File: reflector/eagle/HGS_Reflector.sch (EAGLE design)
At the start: 20 parts, among them J1 U.FL, U1 TQP3M9037, U2 TQP3M903X, U3 LP2985XX-N

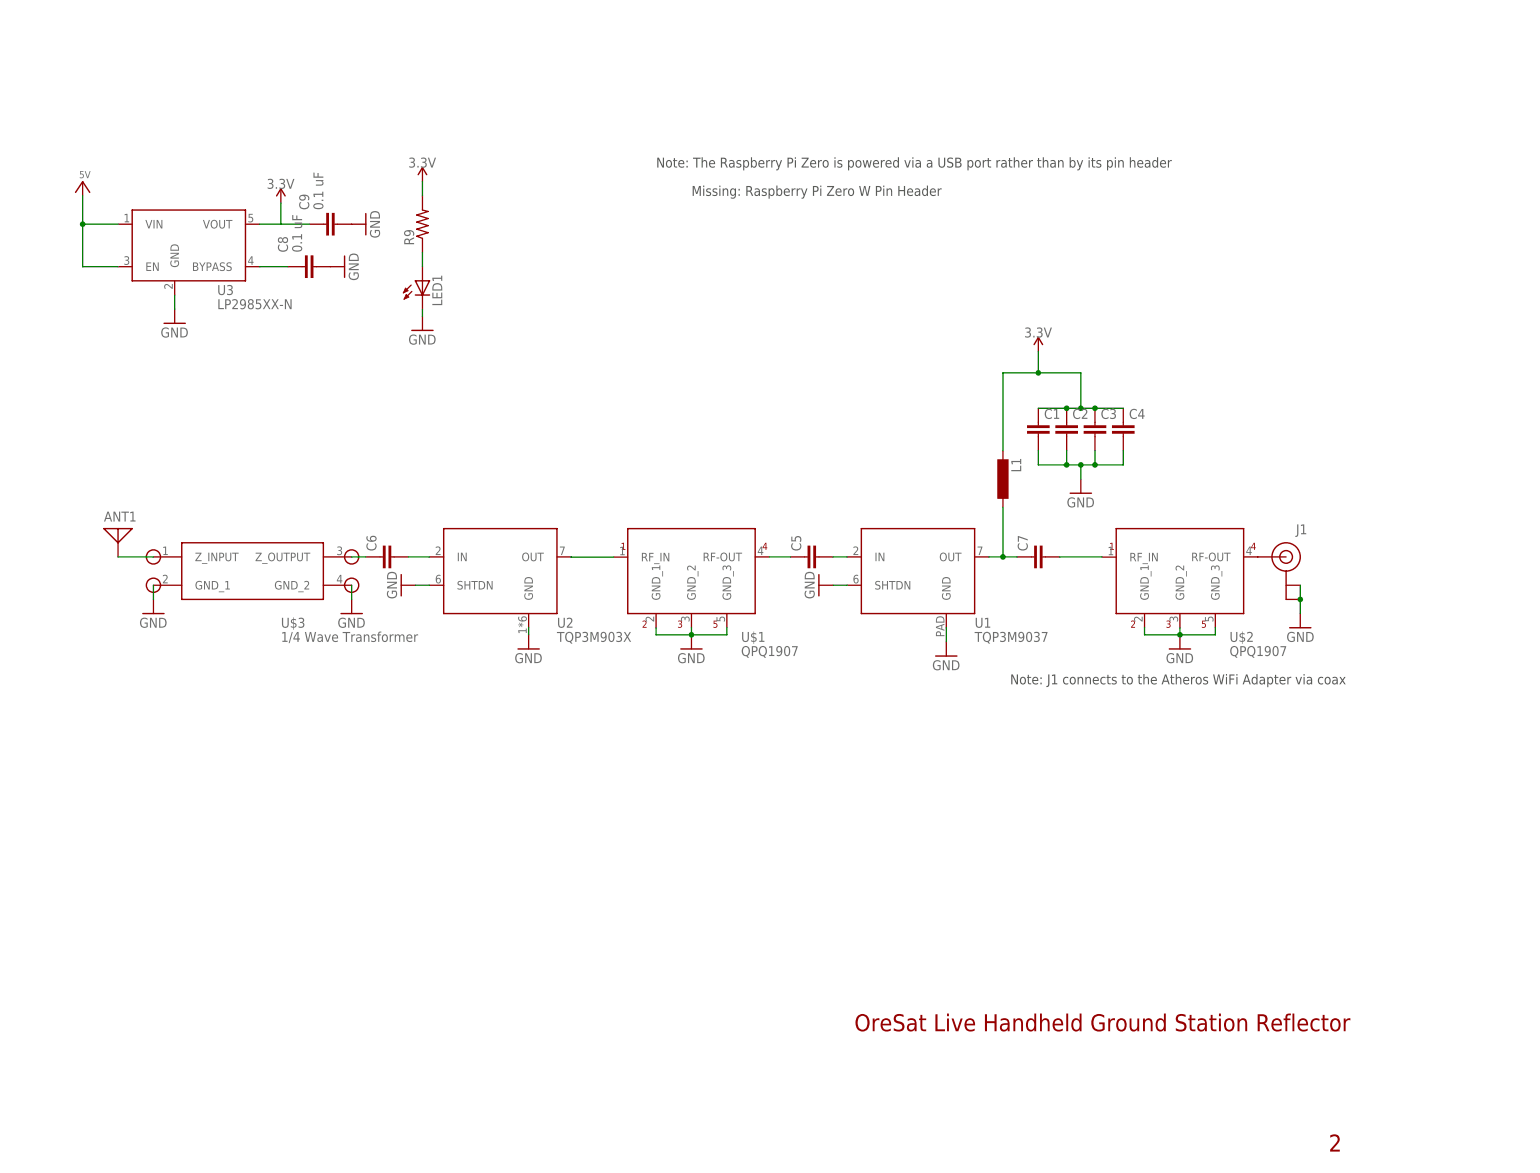
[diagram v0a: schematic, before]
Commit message: Fixed sch/brd inconsistancy
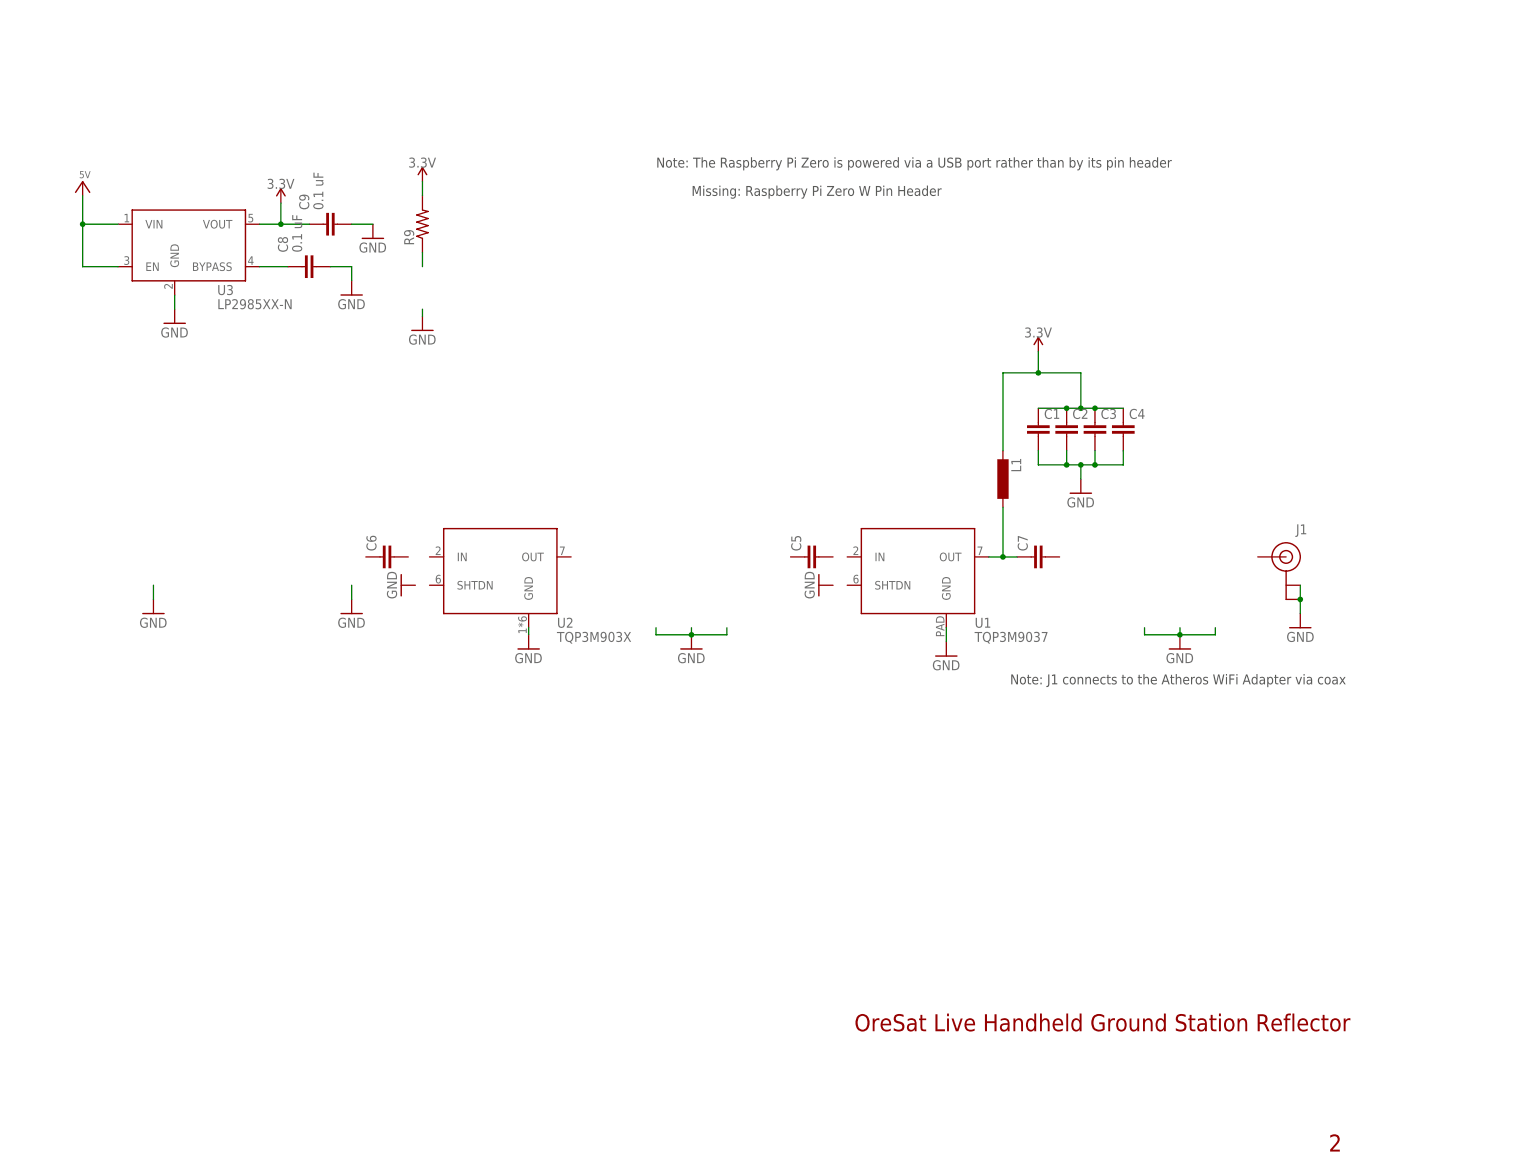
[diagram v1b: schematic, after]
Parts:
- removed ANT1: (no value), discrete:ANTENNA
- removed LED1: (no value), eagle-ltspice:LED_E
- removed U$1, U$2: BPFQPQ1907, HGS_Data_Parts:BPFQPQ1907
- removed U$3: 1/4_WAVE_TRF, HGS_Data_Parts:1/4_WAVE_TRF
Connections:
- removed net N$1 (its old number): C5.2, U1.IN
- removed net N$11: ANT1.1, U$3.Z_INPUT
- removed net N$2: U$1.RF_IN, U2.OUT
- removed net N$3: C5.1, U$1.RF-OUT
- removed net N$4: C7.2
- removed net N$6: J1.SIGNAL, U$2.RF-OUT
- removed net N$7: C6.1, U$3.Z_OUTPUT
- removed net N$8: C6.2, U2.IN
- removed net N$9: U$3.GND_2
- net GND: no longer LED1.C, U$1.GND_1, U$1.GND_2, U$1.GND_3, U$2.GND_1, U$2.GND_2, U$2.GND_3, U$3.GND_1, U1.SHTDN, U2.SHTDN
- net N$10: no longer LED1.A

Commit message: Completed schematic with respect to the current block diagram
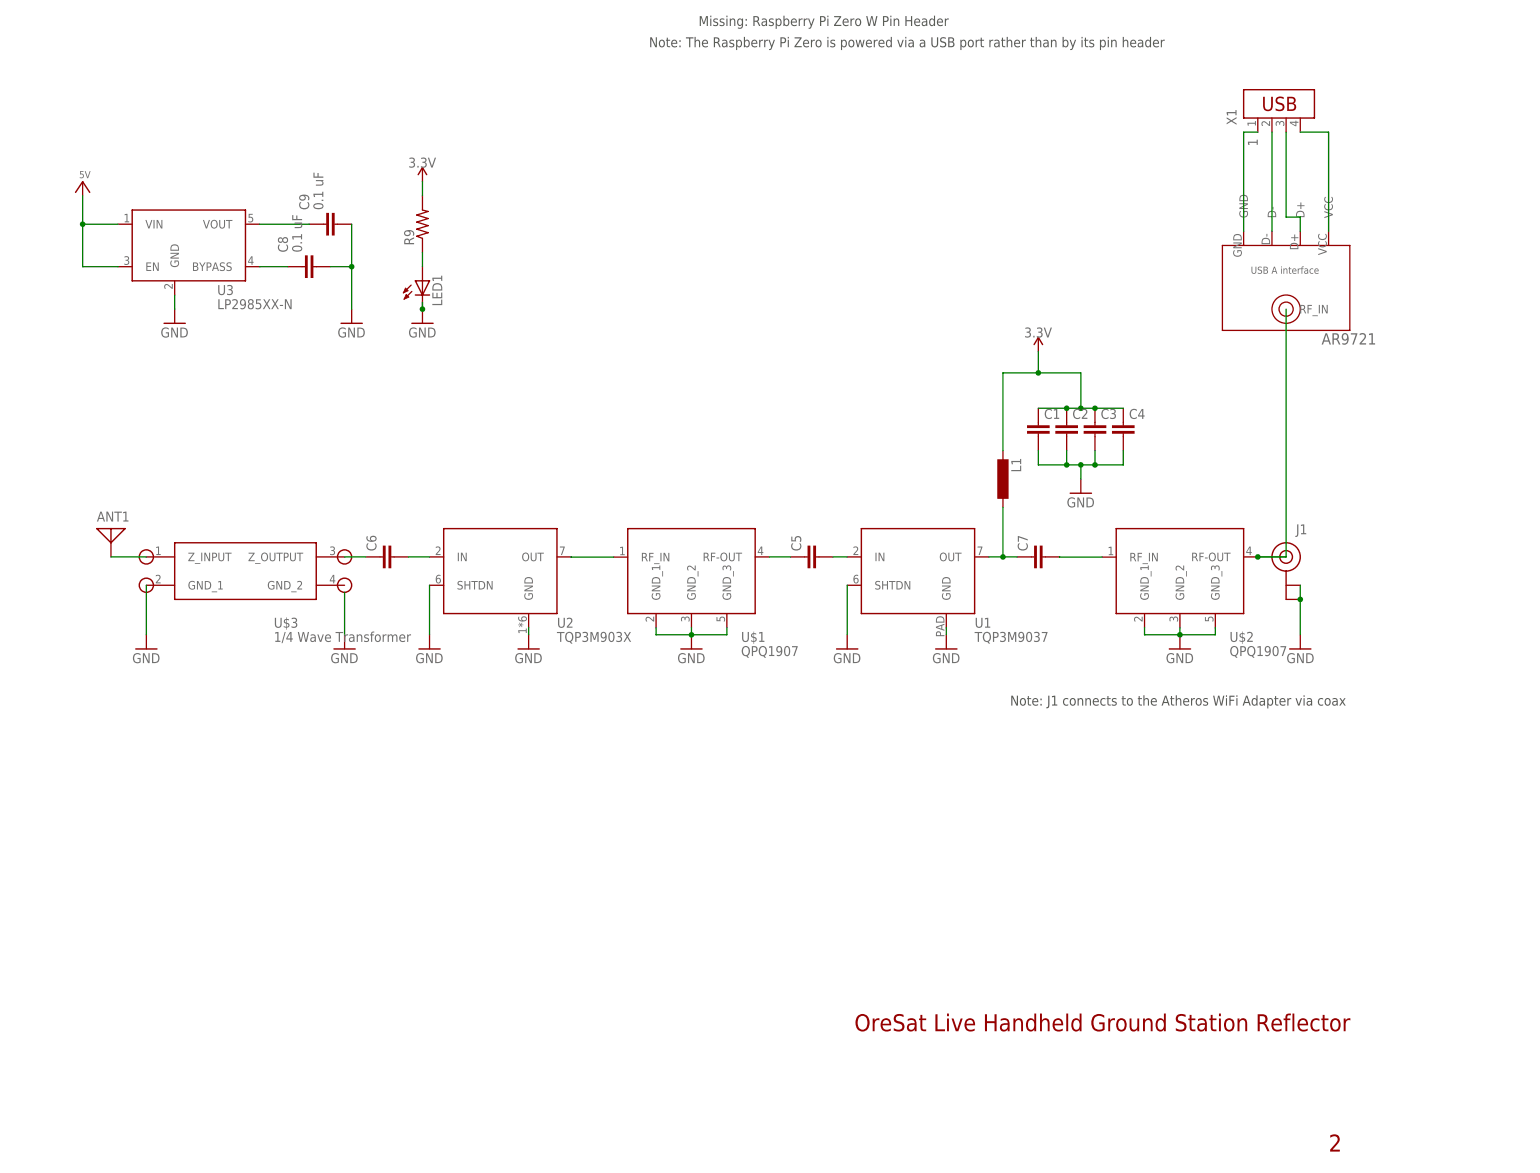
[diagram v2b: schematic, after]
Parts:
- added ANT1: (no value), discrete:ANTENNA
- added LED1: (no value), eagle-ltspice:LED_E
- added U$1, U$2: BPFQPQ1907, HGS_Data_Parts:BPFQPQ1907
- added U$3: 1/4_WAVE_TRF, HGS_Data_Parts:1/4_WAVE_TRF
- added U$4: AR9721, HGS_Data_Parts:AR9721
- added X1: (no value), con-amp:USB-787616
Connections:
- new net 1: X1.1
- new net N$11: C6.2, U2.IN
- new net N$12: ANT1.1, U$3.Z_INPUT
- new net N$14: X1.2
- new net N$15: X1.4
- new net N$16: X1.3
- new net N$2: J1.SIGNAL, U$2.RF-OUT, U$4.RF_IN
- new net N$3: C7.2, U$2.RF_IN
- new net N$4: C5.2, U1.IN
- new net N$7: C5.1, U$1.RF-OUT
- new net N$8: U$1.RF_IN, U2.OUT
- new net N$9: C6.1, U$3.Z_OUTPUT
- net GND: now also LED1.C, U$1.GND_1, U$1.GND_2, U$1.GND_3, U$2.GND_1, U$2.GND_2, U$2.GND_3, U$3.GND_1, U1.SHTDN, U2.SHTDN
- net N$10: now also LED1.A

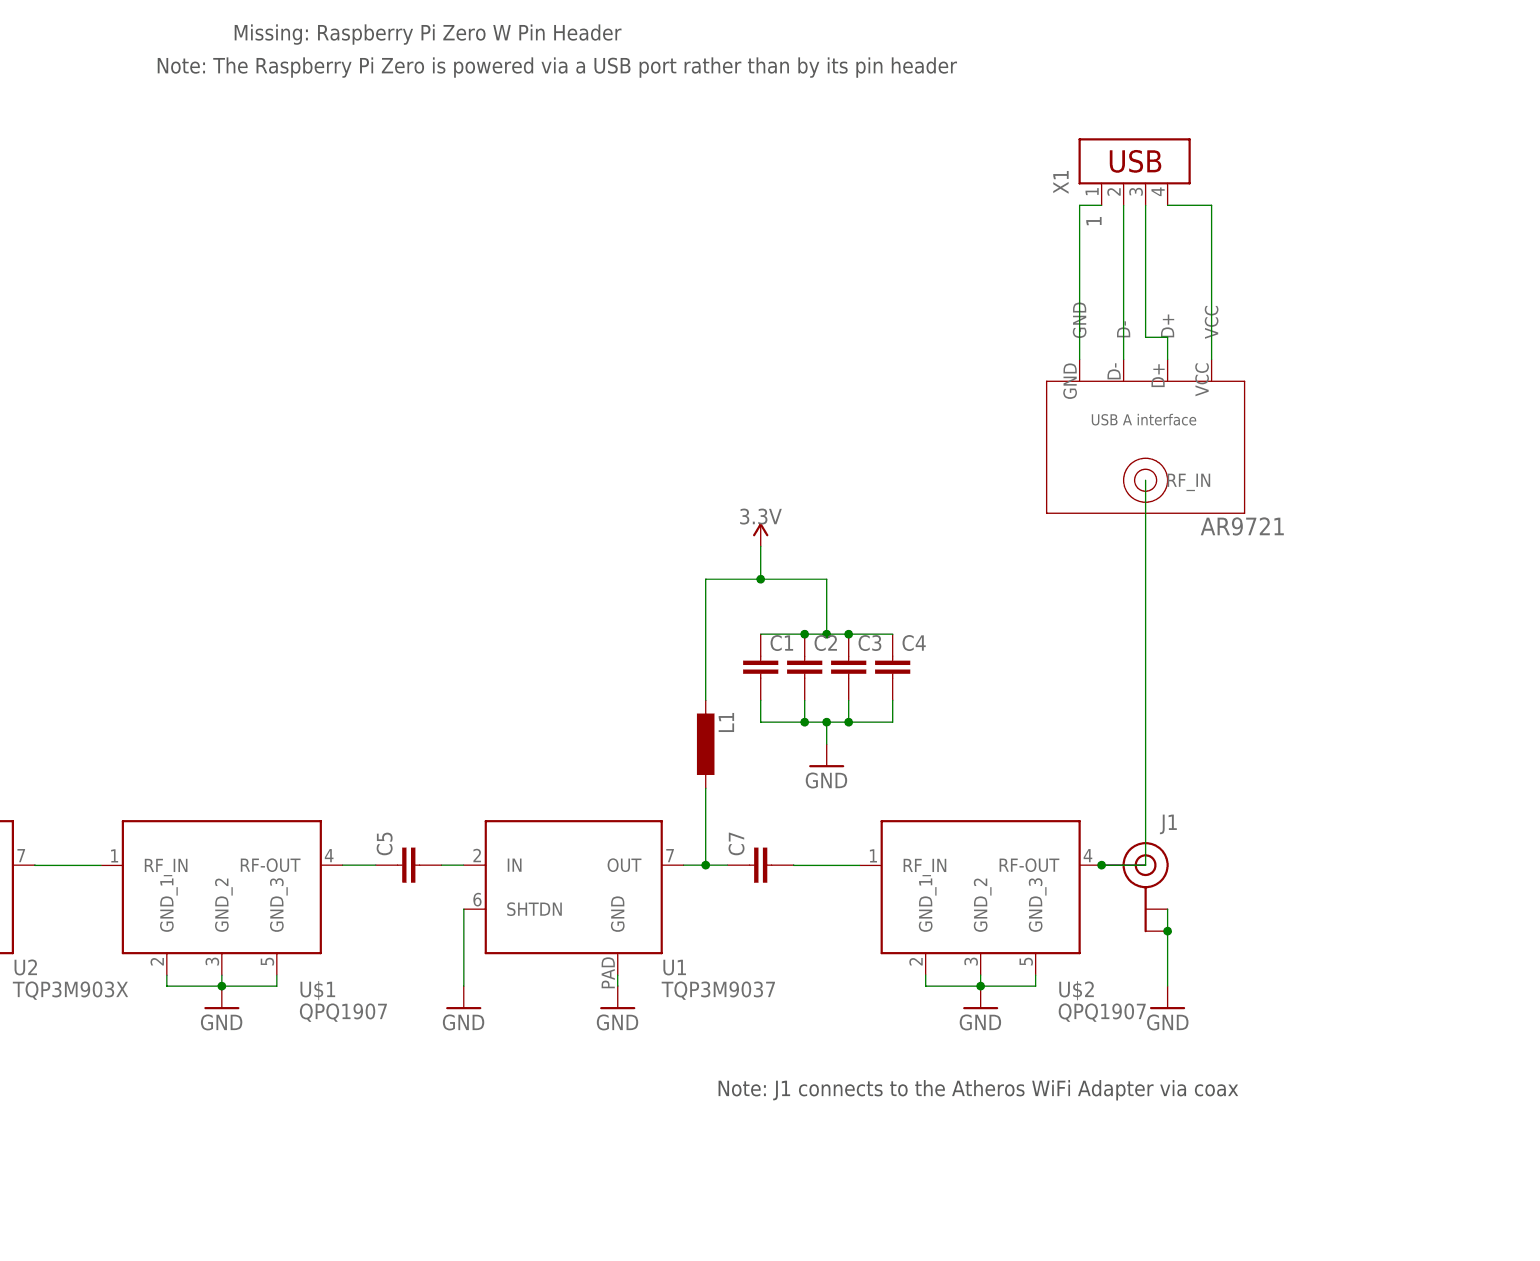
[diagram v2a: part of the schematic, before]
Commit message: Getting rid of unneccesary text
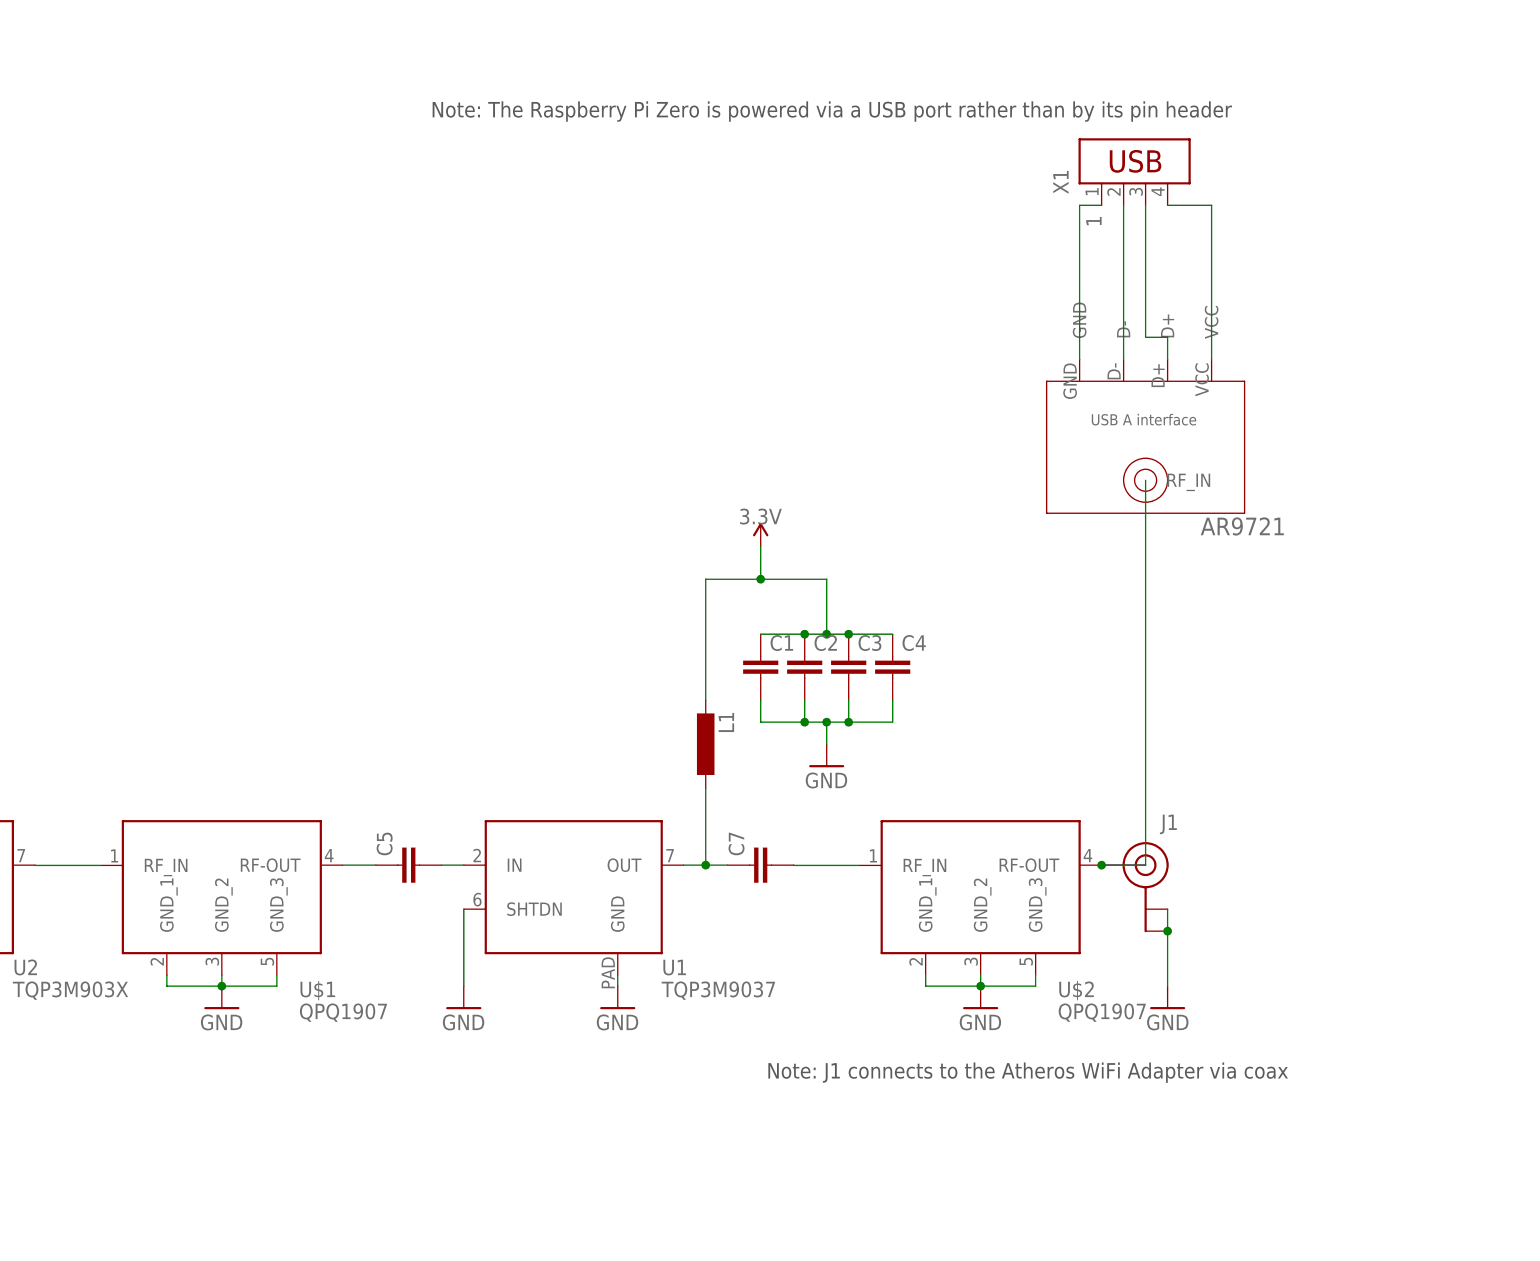
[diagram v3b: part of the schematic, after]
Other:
- note removed: "Missing: Raspberry Pi Zero W Pin Header"
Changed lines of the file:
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@@
 <sheet>
 <plain>
-<text x="152.4" y="208.28" size="1.778" layer="97">Missing: Raspberry Pi Zero W Pin Header</text>
 <text x="180.34" y="27.94" size="3.048" layer="94">OreSat Live Handheld Ground Station Reflector</text>
 <text x="265.43" y="6.35" size="3.048" layer="94">2</text>
-<text x="143.51" y="204.47" size="1.778" layer="97">Note: The Raspberry Pi Zero is powered via a USB port rather than by its pin header</text>
-<text x="208.28" y="86.36" size="1.778" layer="97">Note: J1 connects to the Atheros WiFi Adapter via coax</text>
+<text x="175.26" y="199.39" size="1.778" layer="97">Note: The Raspberry Pi Zero is powered via a USB port rather than by its pin header</text>
+<text x="274.32" y="90.17" size="1.778" layer="97" rot="R180">Note: J1 connects to the Atheros WiFi Adapter via coax</text>
 </plain>
 <instances>
